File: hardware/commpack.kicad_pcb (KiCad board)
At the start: 2 copper layers, 103.8 x 62.5 mm, 23 parts, among them J1 1240COMM, J2 1240COMM_EXT, J3 L8BE-1G1T-91A, U1 SC16C550B, U2 SST39SF010A, U4 AP1117-33, Y1 Crystal

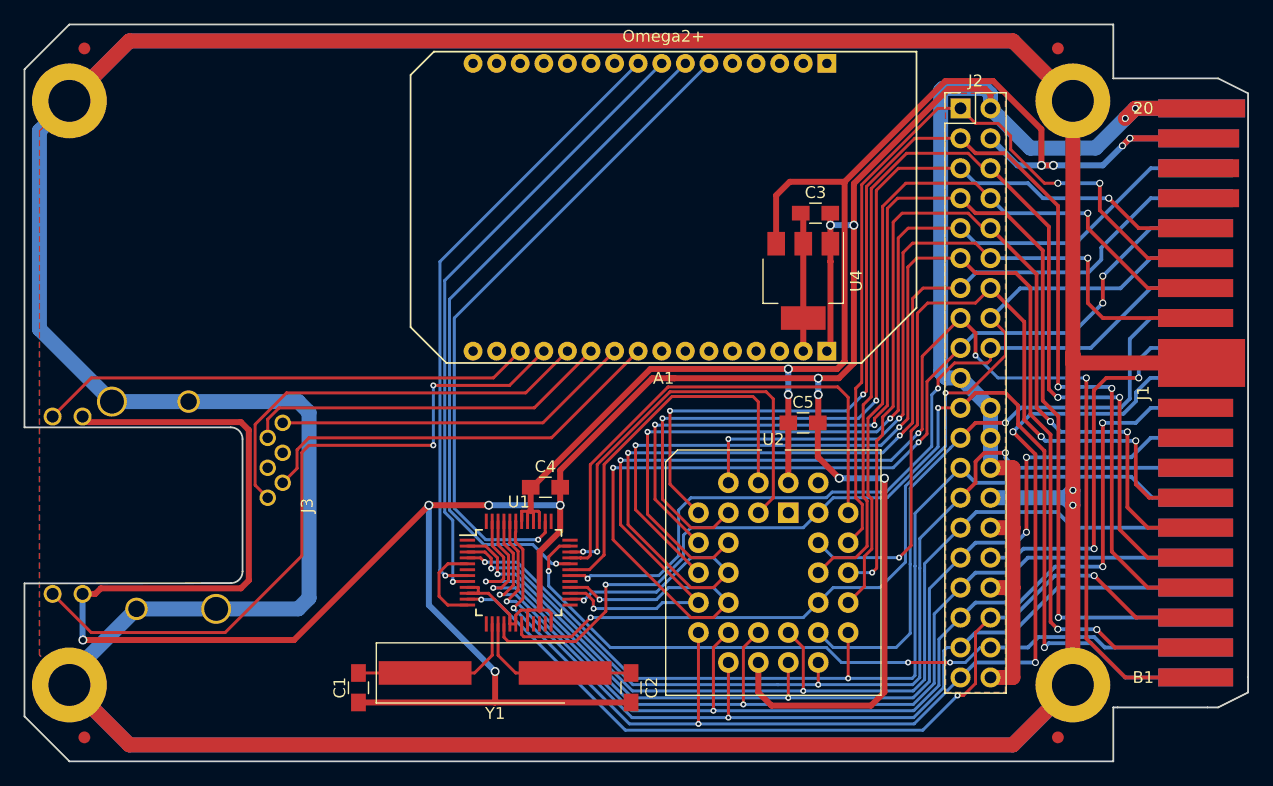
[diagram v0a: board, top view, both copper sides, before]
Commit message: Fix via size on power traces.
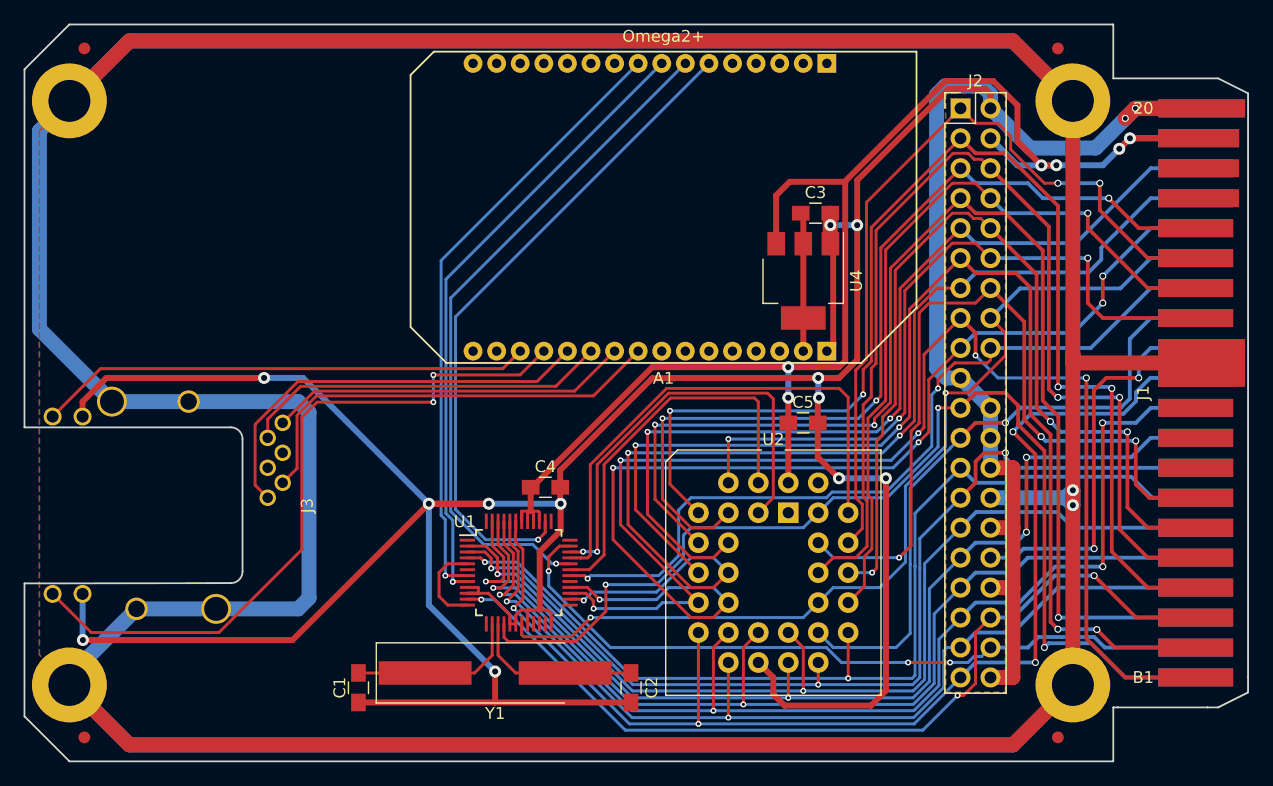
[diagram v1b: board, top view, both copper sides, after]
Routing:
- net /H-A5: track 104.5 -> 101.4 mm
- net /H-A6: track 77.3 -> 74.3 mm
- net /H-A4: track 78.1 -> 75.5 mm
- net /H-A11: track 76.7 -> 74.2 mm
- net /H-A10: track 63.7 -> 61.4 mm
- net /H-A9: track 90.9 -> 88.6 mm
- net /H-A7: track 103.7 -> 101.4 mm
- net GND: track 366.0 -> 368.2 mm, vias 13 -> 14
- net /H-A3: track 100.7 -> 98.5 mm
- net /H-A12: track 59.9 -> 58.0 mm
- net Net-(A1-PadB9): track 35.7 -> 37.4 mm
- net /H-A8: track 66.4 -> 65.3 mm
- net VCC: track 119.2 -> 120.0 mm
- net /H-A2: track 93.5 -> 92.8 mm
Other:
- net class Earth added: clearance 0.1524, trace_width 1.27, via_dia 1.016, via_drill 0.508
- net class Power: via_dia 0.762 -> 1.016

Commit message: Reduce mask expansion to get fingers between UART pads.
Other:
- rule pad_to_mask_clearance: 0.2 -> 0.0762
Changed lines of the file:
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@@
     (pad_size 2 3.8)
     (pad_drill 0)
-    (pad_to_mask_clearance 0.2)
+    (pad_to_mask_clearance 0.0762)
+    (solder_mask_min_width 0.1016)
     (aux_axis_origin 127 118.11)
     (visible_elements FFFEFFFF)

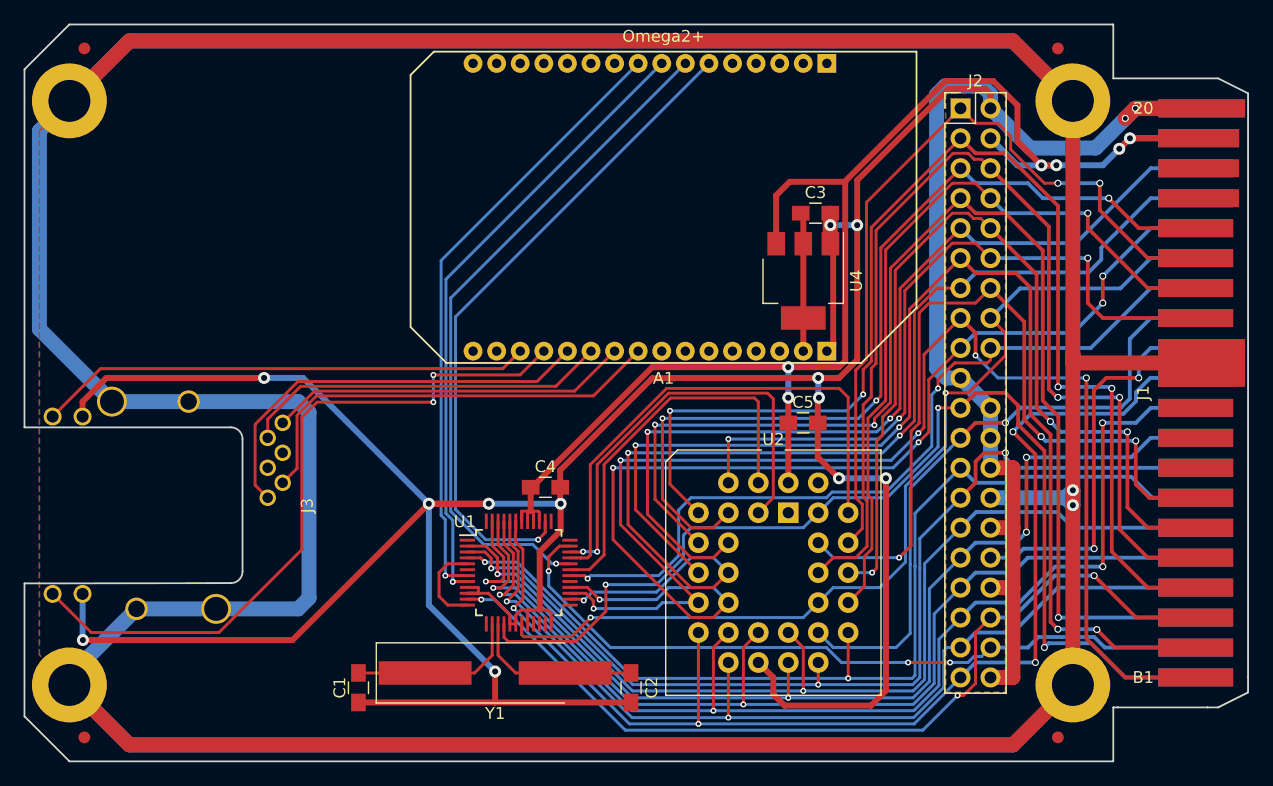
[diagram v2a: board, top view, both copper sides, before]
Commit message: Add a level shifter on the serial lines to the Omega2.
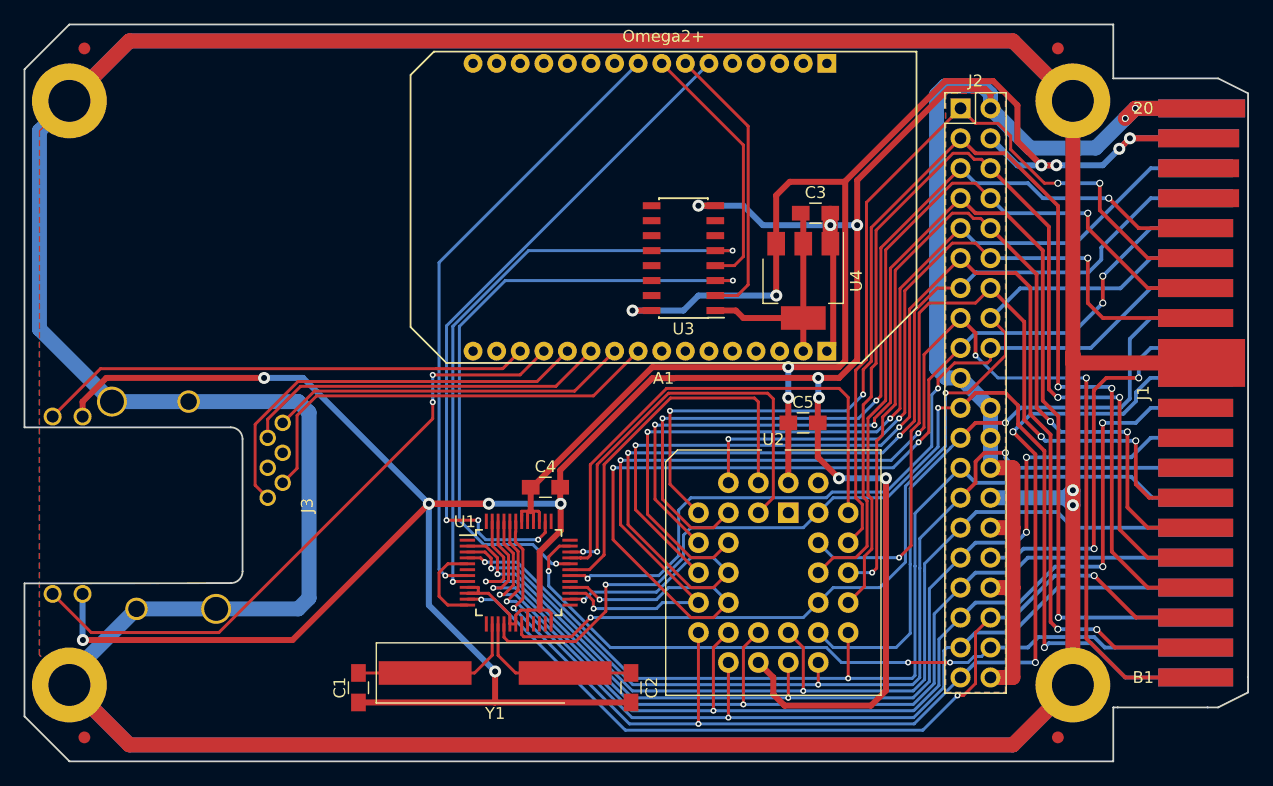
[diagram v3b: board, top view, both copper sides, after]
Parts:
- added U3: HCF4010, Housings_SOIC:SOIC-16_3.9x9.9mm_Pitch1.27mm, F.Cu at (177.8, 77.5)
- Y1: value Crystal -> 22.1184M
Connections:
- A1 pad A7: /A-~CTS -> Net-(A1-PadA7)
- A1 pad A8: /A-RX -> Net-(A1-PadA8)
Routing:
- net Net-(A1-PadA7): track 0.00 -> 24.6 mm
- net Net-(A1-PadA8): track 0.00 -> 21.9 mm
- net VCC: track 120.0 -> 138.7 mm, vias 6 -> 8
- net GND: track 368.2 -> 381.5 mm, vias 14 -> 15
- net +3V3: track 11.8 -> 19.5 mm
- net Net-(A1-PadB13): track 60.8 -> 55.1 mm
- net /A-~CTS: track 58.2 -> 53.6 mm, vias 1 -> 2
- net /A-RX: track 53.0 -> 50.8 mm, vias 1 -> 2
- net /A-~RTS: track 56.6 -> 58.8 mm, vias 1 -> 3

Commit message: Fix alignment of crystal traces.
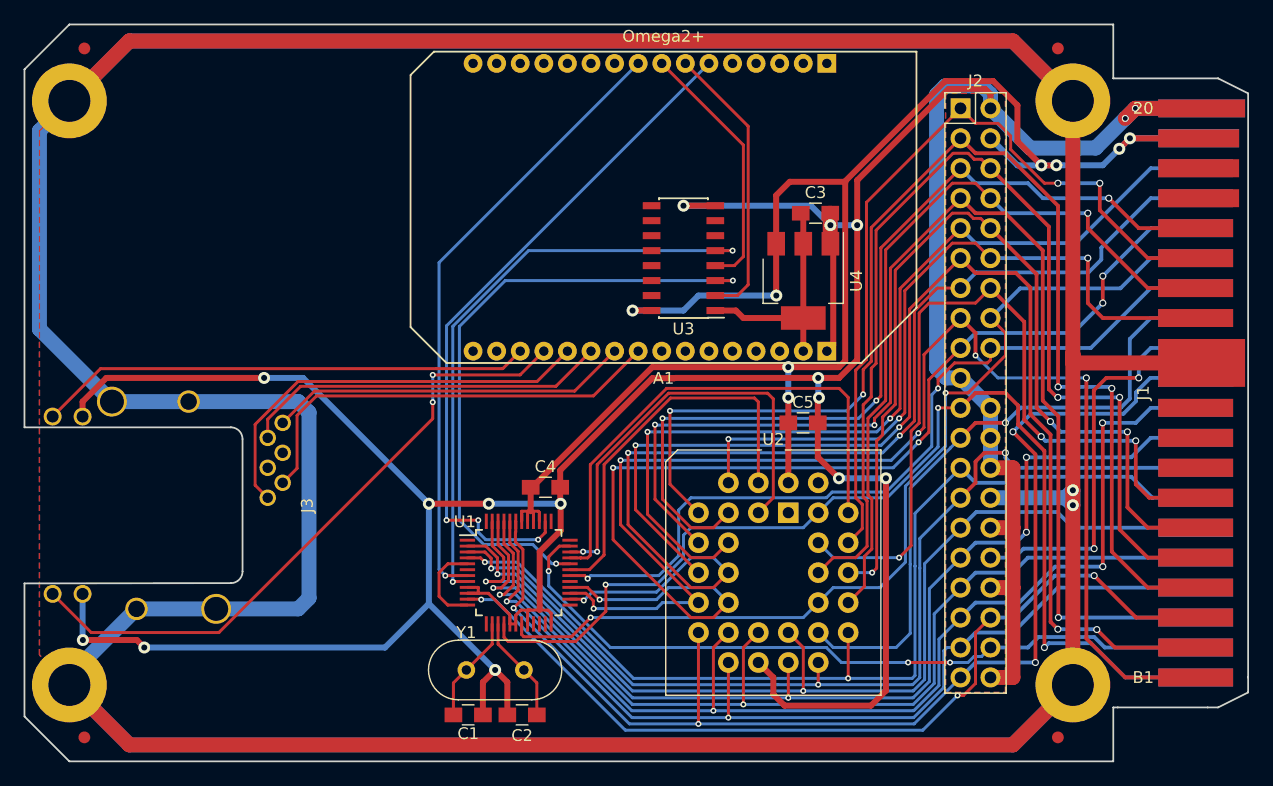
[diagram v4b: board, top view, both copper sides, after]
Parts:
- Y1: footprint Crystals:Crystal_SMD_HC49-SD_HandSoldering -> Crystals:Crystal_HC49-U_Vertical
- moved C1 9.58 mm to (159.5, 116.2), turned to 0 degrees
- moved C2 9.52 mm to (164.1, 116.2), turned to 180 degrees
- moved Y1 2.45 mm to (159.4, 112.4)
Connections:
- A1 pad A7: Net-(A1-PadA7) -> /A-~CTS
- A1 pad A8: Net-(A1-PadA8) -> /A-RX
- U1 pad 32: /A-~CTS -> /U-~RTS
- U1 pad 8: /A-RX -> /U-TX
- U3 pad 2: Net-(A1-PadA7) -> /A-~CTS
- U3 pad 3: /A-~CTS -> /U-~RTS
- U3 pad 4: Net-(A1-PadA8) -> /A-RX
- U3 pad 5: /A-RX -> /U-TX
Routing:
- net /U-~RTS: track 0.00 -> 53.6 mm, vias 0 -> 2
- net /U-TX: track 0.00 -> 50.8 mm, vias 0 -> 2
- net /A-~CTS: track 53.6 -> 24.6 mm, vias 2 -> 0
- net /A-RX: track 50.8 -> 21.9 mm, vias 2 -> 0
- net Net-(A1-PadA7): track 24.6 -> 0.00 mm
- net GND: track 381.5 -> 358.8 mm, vias 15 -> 16
- net Net-(A1-PadA8): track 21.9 -> 0.00 mm
- net Net-(C1-Pad1): track 14.6 -> 9.08 mm
- net Net-(C2-Pad1): track 14.6 -> 9.08 mm

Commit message: Clean up ground planes a bit.
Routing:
- net GND: track 358.8 -> 378.9 mm, vias 16 -> 19
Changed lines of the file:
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@@
     (thickness 1.6)
     (drawings 63)
-    (tracks 977)
+    (tracks 983)
     (zones 0)
     (modules 24)
@@
   (gr_line (start 214.63 115.57) (end 222.25 115.57) (angle 90) (layer Edge.Cuts) (width 0.15))
   (gr_line (start 225.679 113.03) (end 225.679 63.5) (angle 90) (layer Edge.Cuts) (width 0.15))
+  (segment (start 167.386 98.298) (end 176.022 98.298) (width 0.508) (layer B.Cu) (net 1))
+  (segment (start 176.022 98.298) (end 177.8 96.52) (width 0.508) (layer B.Cu) (net 1))
+  (via (at 177.8 96.52) (size 1.016) (drill 0.508) (layers F.Cu B.Cu) (net 1))
+  (segment (start 177.799992 73.025) (end 171.45 66.675008) (width 0.508) (layer F.Cu) (net 1))
+  (segment (start 171.45 66.675008) (end 171.45 66.675) (width 0.508) (layer F.Cu) (net 1))
+  (via (at 171.45 66.675) (size 1.016) (drill 0.508) (layers F.Cu B.Cu) (net 1))
+  (segment (start 149.86 91.948) (end 156.21 98.298) (width 0.508) (layer B.Cu) (net 1))
+  (segment (start 145.542 87.63) (end 149.86 91.948) (width 0.508) (layer B.Cu) (net 1))
+  (via (at 149.86 91.948) (size 1.016) (drill 0.508) (layers F.Cu B.Cu) (net 1))
   (segment (start 162.866 116.205) (end 162.866 113.431) (width 0.508) (layer F.Cu) (net 1) (status 10))
   (segment (start 162.866 113.431) (end 161.83 112.395) (width 0.508) (layer F.Cu) (net 1))
@@
   (segment (start 161.83 112.395) (end 156.21 106.775) (width 0.508) (layer B.Cu) (net 1))
   (segment (start 156.21 106.775) (end 156.21 98.298) (width 0.508) (layer B.Cu) (net 1))
-  (via (at 161.83 112.395) (size 1.016) (drill 0.508) (layers F.Cu B.Cu) (net 1) (status 1000000))
-  (segment (start 145.542 87.63) (end 156.21 98.298) (width 0.508) (layer B.Cu) (net 1))
+  (via (at 161.83 112.395) (size 1.016) (drill 0.508) (layers F.Cu B.Cu) (net 1))
   (segment (start 126.873 109.855) (end 131.445 109.855) (width 0.508) (layer F.Cu) (net 1))
   (segment (start 131.445 109.855) (end 132.08 110.49) (width 0.508) (layer F.Cu) (net 1))
@@
   (segment (start 209.318948 103.632) (end 213.36 103.632) (width 0.32258) (layer B.Cu) (net 21))
   (segment (start 201.295 107.95) (end 202.565 106.68) (width 0.32258) (layer B.Cu) (net 21) (status 10))
-  (segment (start 164.185599 106.356405) (end 163.395572 107.146432) (width 0.254) (layer F.Cu) (net 22))
-  (segment (start 163.550599 101.527666) (end 164.185599 102.162666) (width 0.254) (layer F.Cu) (net 22))
-  (segment (start 163.550599 100.723401) (end 163.550599 101.527666) (width 0.254) (layer F.Cu) (net 22))
-  (segment (start 163.58 100.694) (end 163.550599 100.723401) (width 0.254) (layer F.Cu) (net 22))
-  (segment (start 163.58 99.79) (end 163.58 100.694) (width 0.254) (layer F.Cu) (net 22) (status 10))
+  (segment (start 163.58 99.79) (end 163.58 101.557067) (width 0.254) (layer F.Cu) (net 22) (status 10))
+  (segment (start 163.58 101.557067) (end 164.185599 102.162666) (width 0.254) (layer F.Cu) (net 22))
   (segment (start 164.185599 102.162666) (end 164.185599 106.356405) (width 0.254) (layer F.Cu) (net 22))
+  (segment (start 164.185599 106.356405) (end 163.395572 107.146432) (width 0.254) (layer F.Cu) (net 22))
   (segment (start 173.216168 116.967028) (end 163.395572 107.146432) (width 0.254) (layer B.Cu) (net 22))
   (segment (start 179.07 116.967028) (end 173.216168 116.967028) (width 0.254) (layer B.Cu) (net 22))

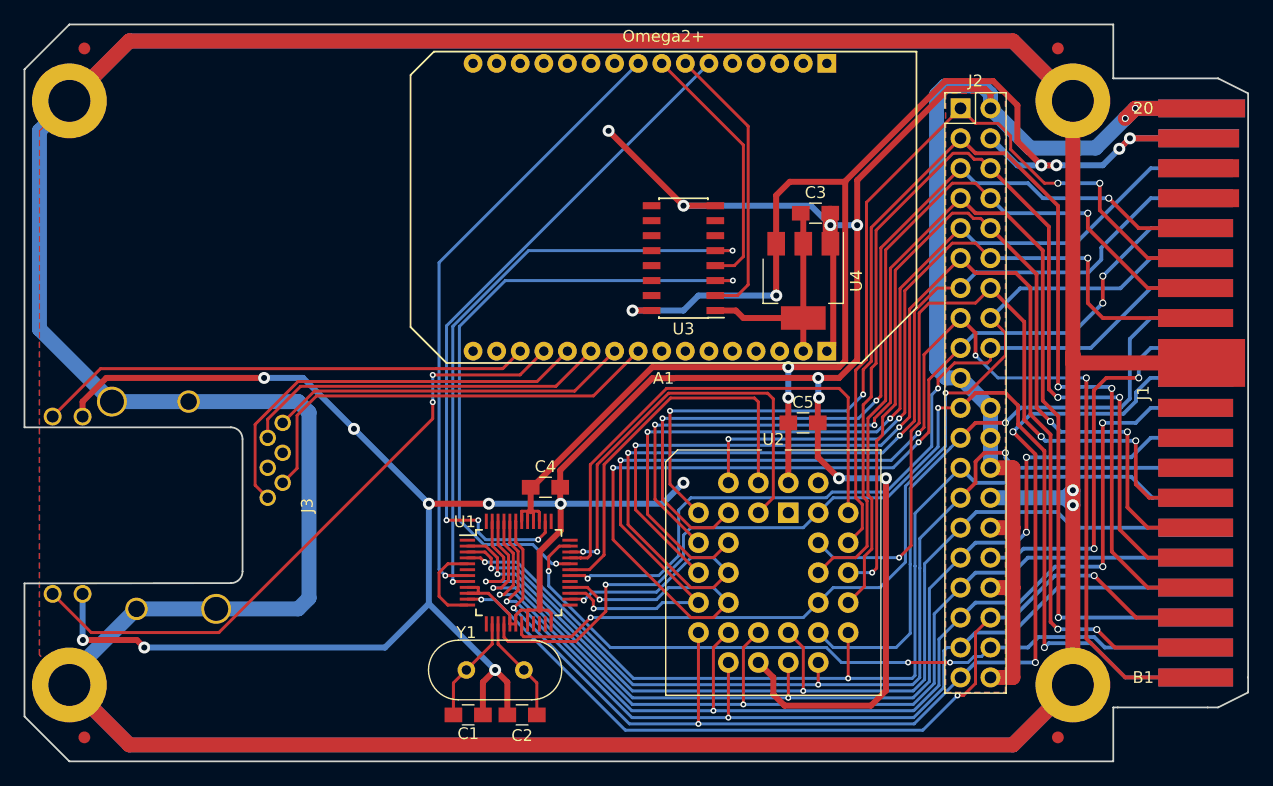
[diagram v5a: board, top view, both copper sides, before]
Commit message: Clean up track with and spacing.
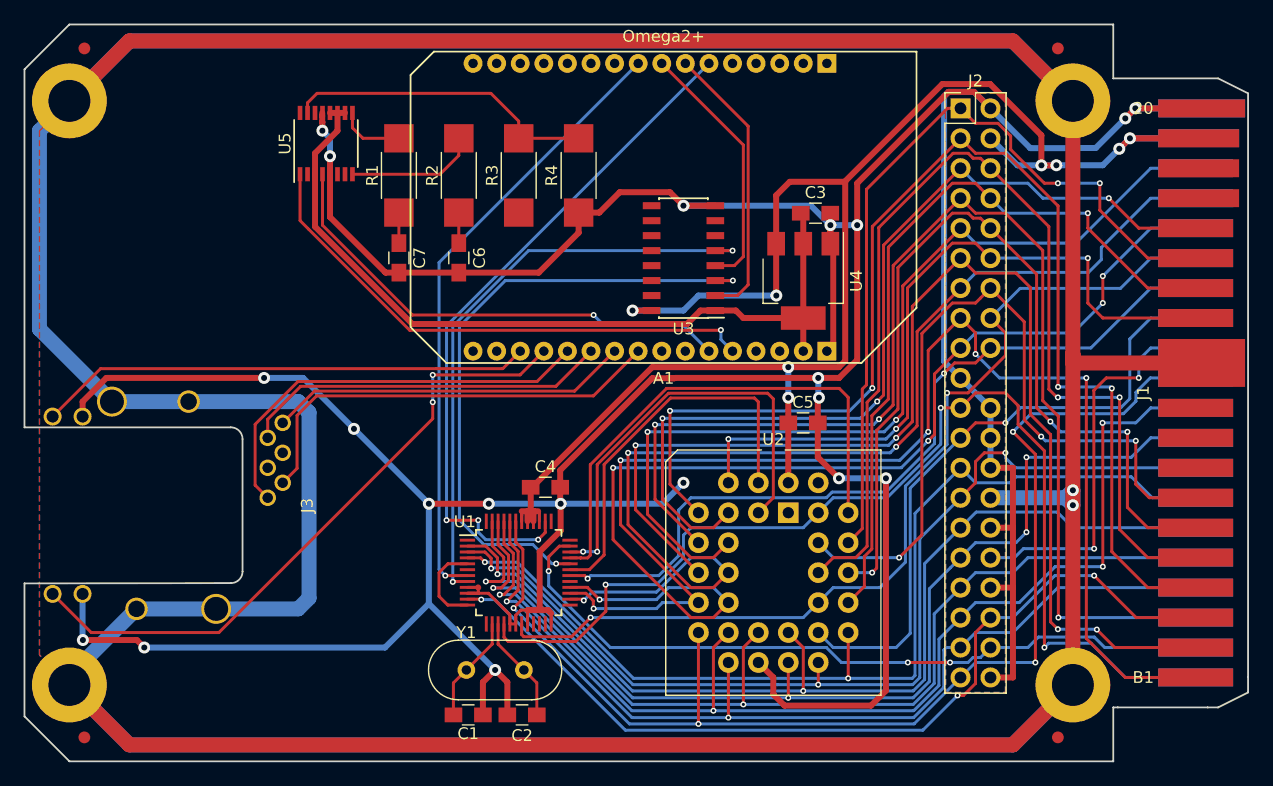
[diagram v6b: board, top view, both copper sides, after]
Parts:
- added C6: 47p, Capacitors_SMD:C_0805_HandSoldering, F.Cu at (158.8, 77.5)
- added C7: 47p, Capacitors_SMD:C_0805_HandSoldering, F.Cu at (153.7, 77.5)
- added R1: 27R, Resistors_SMD:R_2010_HandSoldering, F.Cu at (153.7, 70.5)
- added R2: 27R, Resistors_SMD:R_2010_HandSoldering, F.Cu at (158.8, 70.5)
- added R3: 4k7, Resistors_SMD:R_2010_HandSoldering, F.Cu at (163.8, 70.5)
- added R4: 10k, Resistors_SMD:R_2010_HandSoldering, F.Cu at (168.9, 70.5)
- added U5: FT230XS, Housings_SSOP:SSOP-16_3.9x4.9mm_Pitch0.635mm, F.Cu at (147.5, 67.8)
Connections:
- A1 pad B5: (no net) -> Net-(A1-PadB5)
- A1 pad B6: (no net) -> Net-(A1-PadB6)
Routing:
- net +3V3: track 19.5 -> 69.1 mm
- net Net-(A1-PadB5): track 0.00 -> 45.7 mm, vias 0 -> 1
- net Net-(A1-PadB6): track 0.00 -> 41.5 mm, vias 0 -> 1
- net GND: track 378.9 -> 411.4 mm, vias 19 -> 20
- net Net-(R3-Pad2): track 0.00 -> 26.6 mm
- net Net-(R2-Pad2): track 0.00 -> 11.1 mm
- net Net-(R1-Pad2): track 0.00 -> 5.57 mm
- net Net-(C7-Pad1): track 0.00 -> 2.59 mm
- net Net-(C6-Pad1): track 0.00 -> 2.59 mm
- net /H-A13: track 64.4 -> 63.2 mm
- net /H-A2: track 92.8 -> 92.0 mm
- net /H-INT: track 66.1 -> 65.5 mm
- net VCC: track 138.7 -> 138.2 mm
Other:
- rule via_min_size: 0.254 -> 0.508
